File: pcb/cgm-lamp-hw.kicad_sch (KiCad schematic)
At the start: 55 parts, among them J1 USB_C_Receptacle_USB2.0_14P, J2 Conn_01x02, J3 DNP, Q1 DMG2305, SW1 RotaryEncoder_Switch_MP, SW2 SW_Push, SW3 SW_Push, SW4 SW_SPST, U1 RT9080-33GJ5, U2 MCP73831-2-OT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

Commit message: Assign footprints, start layout
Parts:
- C1, C10, C11, C2, C3, C4, C5, C6, C7, C8, C9: footprint (none) -> Capacitor_SMD:C_0603_1608Metric_Pad1.08x0.95mm_HandSolder
- D10: footprint (none) -> Diode_SMD:D_SOD-323_HandSoldering
- D11, D12, D13, D9: footprint (none) -> LED_SMD:LED_1206_3216Metric_Pad1.42x1.75mm_HandSolder
- J1: footprint (none) -> Connector_USB:USB_C_Receptacle_GCT_USB4105-xx-A_16P_TopMnt_Horizontal
- J2: footprint (none) -> Connector_JST:JST_PH_S2B-PH-SM4-TB_1x02-1MP_P2.00mm_Horizontal
- J3: footprint (none) -> Connector_PinHeader_2.54mm:PinHeader_1x03_P2.54mm_Vertical
- R1, R10, R11, R12, R13, R14, R15, R16, R17, R2, R3, R4, R5, R6, R7, R8, R9: footprint (none) -> Resistor_SMD:R_0603_1608Metric_Pad0.98x0.95mm_HandSolder
- SW1: footprint (none) -> Rotary_Encoder:RotaryEncoder_Bourns_Vertical_PEC12R-3x17F-Sxxxx
- SW2, SW3: footprint (none) -> Button_Switch_SMD:SW_SPST_PTS645
- SW4: footprint (none) -> Button_Switch_THT:SW_E-Switch_EG2219_DPDT_Angled
- TP1, TP2: footprint (none) -> TestPoint:TestPoint_Loop_D2.54mm_Drill1.5mm_Beaded
- U1: footprint RT9080-33GJ5:SOT94P280X100-5N -> SnapEDA:SOT94P280X100-5N
- U3: footprint ESP32-C6-WROOM-1-N8:XCVR_ESP32-C6-WROOM-1-N8 -> SnapEDA:XCVR_ESP32-C6-WROOM-1-N8
- U4: footprint MAX17048G_T10:SON50P200X200X80-9N -> SnapEDA:SON50P200X200X80-9N
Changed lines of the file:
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@@
 			)
 		)
-		(property "Footprint" ""
+		(property "Footprint" "Resistor_SMD:R_0603_1608Metric_Pad0.98x0.95mm_HandSolder"
 			(at 99.822 144.78 90)
 			(effects
@@
 			)
 		)
-		(property "Footprint" ""
+		(property "Footprint" "Resistor_SMD:R_0603_1608Metric_Pad0.98x0.95mm_HandSolder"
 			(at 140.208 179.07 90)
 			(effects
@@
 			)
 		)
-		(property "Footprint" ""
+		(property "Footprint" "Resistor_SMD:R_0603_1608Metric_Pad0.98x0.95mm_HandSolder"
 			(at 215.138 48.26 90)
 			(effects
@@
 			)
 		)
-		(property "Footprint" ""
+		(property "Footprint" "LED_SMD:LED_1206_3216Metric_Pad1.42x1.75mm_HandSolder"
 			(at 138.43 187.96 0)
 			(effects
@@
 			)
 		)
-		(property "Footprint" ""
+		(property "Footprint" "Resistor_SMD:R_0603_1608Metric_Pad0.98x0.95mm_HandSolder"
 			(at 51.562 36.83 90)
 			(effects
@@
 			)
 		)
-		(property "Footprint" ""
+		(property "Footprint" "Resistor_SMD:R_0603_1608Metric_Pad0.98x0.95mm_HandSolder"
 			(at 173.228 140.97 90)
 			(effects
@@
 			)
 		)
-		(property "Footprint" ""
+		(property "Footprint" "Resistor_SMD:R_0603_1608Metric_Pad0.98x0.95mm_HandSolder"
 			(at 166.878 179.07 90)
 			(effects
@@
 			)
 		)
-		(property "Footprint" ""
+		(property "Footprint" "Resistor_SMD:R_0603_1608Metric_Pad0.98x0.95mm_HandSolder"
 			(at 104.648 187.96 90)
 			(effects
@@
 			)
 		)
-		(property "Footprint" ""
+		(property "Footprint" "Resistor_SMD:R_0603_1608Metric_Pad0.98x0.95mm_HandSolder"
 			(at 118.11 52.578 90)
 			(effects
@@
 			)
 		)
-		(property "Footprint" ""
+		(property "Footprint" "LED_SMD:LED_1206_3216Metric_Pad1.42x1.75mm_HandSolder"
 			(at 165.1 187.96 0)
 			(effects
@@
 			)
 		)
-		(property "Footprint" ""
+		(property "Footprint" "Resistor_SMD:R_0603_1608Metric_Pad0.98x0.95mm_HandSolder"
 			(at 117.348 187.96 90)
 			(effects
@@
 			)
 		)
-		(property "Footprint" ""
+		(property "Footprint" "Resistor_SMD:R_0603_1608Metric_Pad0.98x0.95mm_HandSolder"
 			(at 168.91 88.392 90)
 			(effects
@@
 			)
 		)
-		(property "Footprint" ""
+		(property "Footprint" "LED_SMD:LED_1206_3216Metric_Pad1.42x1.75mm_HandSolder"
 			(at 201.93 48.26 0)
 			(effects
@@
 			)
 		)
-		(property "Footprint" ""
+		(property "Footprint" "Capacitor_SMD:C_0603_1608Metric_Pad1.08x0.95mm_HandSolder"
 			(at 225.7552 101.6 0)
 			(effects
@@
 			)
 		)
-		(property "Footprint" ""
+		(property "Footprint" "Resistor_SMD:R_0603_1608Metric_Pad0.98x0.95mm_HandSolder"
 			(at 243.078 48.26 90)
 			(effects
@@
 			)
 		)
-		(property "Footprint" ""
+		(property "Footprint" "Diode_SMD:D_SOD-323_HandSoldering"
 			(at 96.52 45.72 0)
 			(effects
@@
 			)
 		)
-		(property "Footprint" ""
+		(property "Footprint" "Button_Switch_THT:SW_E-Switch_EG2219_DPDT_Angled"
 			(at 250.19 152.4 0)
 			(effects
@@
 			)
 		)
-		(property "Footprint" ""
+		(property "Footprint" "Button_Switch_SMD:SW_SPST_PTS645"
 			(at 166.37 152.4 0)
 			(effects
@@
 			)
 		)
-		(property "Footprint" "ESP32-C6-WROOM-1-N8:XCVR_ESP32-C6-WROOM-1-N8"
+		(property "Footprint" "SnapEDA:XCVR_ESP32-C6-WROOM-1-N8"
 			(at 128.27 109.22 0)
 			(effects
@@
 			)
 		)
-		(property "Footprint" ""
+		(property "Footprint" "Capacitor_SMD:C_0603_1608Metric_Pad1.08x0.95mm_HandSolder"
 			(at 186.3852 156.21 0)
 			(effects
@@
 			)
 		)
-		(property "Footprint" ""
+		(property "Footprint" "Connector_USB:USB_C_Receptacle_GCT_USB4105-xx-A_16P_TopMnt_Horizontal"
 			(at 33.02 40.64 0)
 			(effects
@@
 			)
 		)
-		(property "Footprint" ""
+		(property "Footprint" "Connector_JST:JST_PH_S2B-PH-SM4-TB_1x02-1MP_P2.00mm_Horizontal"
 			(at 266.7 38.1 0)
 			(effects
@@
 			)
 		)
-		(property "Footprint" ""
+		(property "Footprint" "TestPoint:TestPoint_Loop_D2.54mm_Drill1.5mm_Beaded"
 			(at 149.86 111.76 0)
 			(effects
@@
 			)
 		)
-		(property "Footprint" ""
+		(property "Footprint" "Resistor_SMD:R_0603_1608Metric_Pad0.98x0.95mm_HandSolder"
 			(at 202.692 104.14 90)
 			(effects
@@
 			)
 		)
-		(property "Footprint" ""
+		(property "Footprint" "Resistor_SMD:R_0603_1608Metric_Pad0.98x0.95mm_HandSolder"
 			(at 87.122 52.07 90)
 			(effects
@@
 			)
 		)
-		(property "Footprint" "RT9080-33GJ5:SOT94P280X100-5N"
+		(property "Footprint" "SnapEDA:SOT94P280X100-5N"
 			(at 123.19 45.72 0)
 			(effects
@@
 			)
 		)
-		(property "Footprint" ""
+		(property "Footprint" "Capacitor_SMD:C_0603_1608Metric_Pad1.08x0.95mm_HandSolder"
 			(at 108.9152 55.88 0)
 			(effects
@@
 			)
 		)
-		(property "Footprint" ""
+		(property "Footprint" "Button_Switch_SMD:SW_SPST_PTS645"
 			(at 205.74 152.4 0)
 			(effects
@@
 			)
 		)
-		(property "Footprint" ""
+		(property "Footprint" "Resistor_SMD:R_0603_1608Metric_Pad0.98x0.95mm_HandSolder"
 			(at 154.178 179.07 90)
 			(effects
@@
 			)
 		)
-		(property "Footprint" ""
+		(property "Footprint" "Connector_PinHeader_2.54mm:PinHeader_1x03_P2.54mm_Vertical"
 			(at 16.51 153.67 0)
 			(effects
@@
 			)
 		)
-		(property "Footprint" ""
+		(property "Footprint" "Resistor_SMD:R_0603_1608Metric_Pad0.98x0.95mm_HandSolder"
 			(at 268.732 85.09 90)
 			(effects
@@
 			)
 		)
-		(property "Footprint" ""
+		(property "Footprint" "LED_SMD:LED_1206_3216Metric_Pad1.42x1.75mm_HandSolder"
 			(at 152.4 187.96 0)
 			(effects
@@
 			)
 		)
-		(property "Footprint" ""
+		(property "Footprint" "Capacitor_SMD:C_0603_1608Metric_Pad1.08x0.95mm_HandSolder"
 			(at 191.4652 46.99 0)
 			(effects
@@
 			)
 		)
-		(property "Footprint" ""
+		(property "Footprint" "Resistor_SMD:R_0603_1608Metric_Pad0.98x0.95mm_HandSolder"
 			(at 64.262 36.83 90)
 			(effects
@@
 			)
 		)
-		(property "Footprint" ""
+		(property "Footprint" "Capacitor_SMD:C_0603_1608Metric_Pad1.08x0.95mm_HandSolder"
 			(at 174.2948 91.44 0)
 			(effects
@@
 			)
 		)
-		(property "Footprint" ""
+		(property "Footprint" "Rotary_Encoder:RotaryEncoder_Bourns_Vertical_PEC12R-3x17F-Sxxxx"
 			(at 183.896 105.41 0)
 			(effects
@@
 			)
 		)
-		(property "Footprint" ""
+		(property "Footprint" "Capacitor_SMD:C_0603_1608Metric_Pad1.08x0.95mm_HandSolder"
 			(at 252.4252 52.07 0)
 			(effects
@@
 			)
 		)
-		(property "Footprint" ""
+		(property "Footprint" "Capacitor_SMD:C_0603_1608Metric_Pad1.08x0.95mm_HandSolder"
 			(at 165.4048 110.49 0)
 			(effects
@@
 			)
 		)
-		(property "Footprint" ""
+		(property "Footprint" "TestPoint:TestPoint_Loop_D2.54mm_Drill1.5mm_Beaded"
 			(at 149.86 114.3 0)
 			(effects
@@
 			)
 		)
-		(property "Footprint" "MAX17048G_T10:SON50P200X200X80-9N"
+		(property "Footprint" "SnapEDA:SON50P200X200X80-9N"
 			(at 250.19 104.14 0)
 			(effects
@@
 			)
 		)
-		(property "Footprint" ""
+		(property "Footprint" "Capacitor_SMD:C_0603_1608Metric_Pad1.08x0.95mm_HandSolder"
 			(at 266.3952 156.21 0)
 			(effects
@@
 			)
 		)
-		(property "Footprint" ""
+		(property "Footprint" "Resistor_SMD:R_0603_1608Metric_Pad0.98x0.95mm_HandSolder"
 			(at 164.592 104.14 90)
 			(effects
@@
 			)
 		)
-		(property "Footprint" ""
+		(property "Footprint" "Capacitor_SMD:C_0603_1608Metric_Pad1.08x0.95mm_HandSolder"
 			(at 225.7552 156.21 0)
 			(effects
@@
 			)
 		)
-		(property "Footprint" ""
+		(property "Footprint" "Capacitor_SMD:C_0603_1608Metric_Pad1.08x0.95mm_HandSolder"
 			(at 203.5048 110.49 0)
 			(effects
@@
 			)
 		)
-		(property "Footprint" ""
+		(property "Footprint" "Capacitor_SMD:C_0603_1608Metric_Pad1.08x0.95mm_HandSolder"
 			(at 158.4452 55.88 0)
 			(effects

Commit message: Add dru, more layout
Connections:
- net ENC_A: now also U3.16 (IO18); no longer U3.27 (IO2)
- net ENC_B: now also U3.17 (IO19); no longer U3.26 (IO3)
- net ENC_BTN: now also U3.14 (IO13); no longer U3.9 (IO1)
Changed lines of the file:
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@@
+	)
+	(no_connect
+		(at 107.95 106.68)
 	)
 	(no_connect
@@
 	)
 	(no_connect
-		(at 148.59 101.6)
-	)
-	(no_connect
-		(at 148.59 114.3)
-	)
-	(no_connect
 		(at 107.95 99.06)
 	)
@@
 	)
 	(no_connect
-		(at 148.59 111.76)
+		(at 107.95 101.6)
+	)
+	(no_connect
+		(at 107.95 104.14)
 	)
 	(no_connect
@@
 		)
 	)
+	(wire
+		(pts
+			(xy 148.59 114.3) (xy 157.48 114.3)
+		)
+		(stroke
+			(width 0)
+			(type default)
+		)
+	)
 	(polyline
 		(pts
@@
 	(wire
 		(pts
-			(xy 99.06 101.6) (xy 107.95 101.6)
-		)
-		(stroke
-			(width 0)
-			(type default)
-		)
-	)
-	(wire
-		(pts
-			(xy 99.06 104.14) (xy 107.95 104.14)
+			(xy 148.59 111.76) (xy 157.48 111.76)
 		)
 		(stroke
@@
 	(wire
 		(pts
-			(xy 99.06 106.68) (xy 107.95 106.68)
-		)
-		(stroke
-			(width 0)
-			(type default)
-		)
-	)
-	(wire
-		(pts
 			(xy 97.79 195.58) (xy 102.87 195.58)
 		)
@@
 		(pts
 			(xy 274.32 104.14) (xy 267.97 104.14)
+		)
+		(stroke
+			(width 0)
+			(type default)
+		)
+	)
+	(wire
+		(pts
+			(xy 148.59 101.6) (xy 157.48 101.6)
 		)
 		(stroke
@@
 	(label "CHG"
 		(at 99.06 109.22 0)
+		(fields_autoplaced yes)
 		(effects
 			(font
@@
 	(label "ENC_B"
 		(at 190.5 118.11 90)
+		(fields_autoplaced yes)
 		(effects
 			(font
@@
 	(label "VREG_EN"
 		(at 274.32 146.05 180)
+		(fields_autoplaced yes)
 		(effects
 			(font
@@
 	(label "BOOT"
 		(at 232.41 146.05 180)
+		(fields_autoplaced yes)
 		(effects
 			(font
@@
 	(label "RGB"
 		(at 107.95 151.13 180)
+		(fields_autoplaced yes)
 		(effects
 			(font
@@
 	)
 	(label "ENC_BTN"
-		(at 99.06 101.6 0)
-		(effects
-			(font
-				(size 1.27 1.27)
-			)
-			(justify left bottom)
+		(at 157.48 101.6 180)
+		(fields_autoplaced yes)
+		(effects
+			(font
+				(size 1.27 1.27)
+			)
+			(justify right bottom)
 		)
 	)
 	(label "RGB"
 		(at 99.06 119.38 0)
+		(fields_autoplaced yes)
 		(effects
 			(font
@@
 	(label "D+"
 		(at 157.48 99.06 180)
+		(fields_autoplaced yes)
 		(effects
 			(font
@@
 	(label "ALERT"
 		(at 157.48 172.72 180)
+		(fields_autoplaced yes)
 		(effects
 			(font
@@
 	(label "D-"
 		(at 48.26 39.37 180)
+		(fields_autoplaced yes)
 		(effects
 			(font
@@
 	(label "ALERT"
 		(at 279.4 91.44 180)
+		(fields_autoplaced yes)
 		(effects
 			(font
@@
 	(label "VREG_EN"
 		(at 114.3 54.61 0)
+		(fields_autoplaced yes)
 		(effects
 			(font
@@
 	(label "SDA"
 		(at 99.06 114.3 0)
+		(fields_autoplaced yes)
 		(effects
 			(font
@@
 	(label "VBAT"
 		(at 217.17 91.44 0)
+		(fields_autoplaced yes)
 		(effects
 			(font
@@
 	(label "RGB"
 		(at 26.67 156.21 180)
+		(fields_autoplaced yes)
 		(effects
 			(font
@@
 	(label "ESP_EN"
 		(at 193.04 146.05 180)
+		(fields_autoplaced yes)
 		(effects
 			(font
@@
 	(label "SCL"
 		(at 99.06 116.84 0)
+		(fields_autoplaced yes)
 		(effects
 			(font
@@
 	(label "SDA"
 		(at 97.79 195.58 0)
+		(fields_autoplaced yes)
 		(effects
 			(font
@@
 	)
 	(label "ENC_B"
-		(at 99.06 106.68 0)
-		(effects
-			(font
-				(size 1.27 1.27)
-			)
-			(justify left bottom)
+		(at 157.48 114.3 180)
+		(fields_autoplaced yes)
+		(effects
+			(font
+				(size 1.27 1.27)
+			)
+			(justify right bottom)
 		)
 	)
 	(label "ENC_A"
-		(at 99.06 104.14 0)
-		(effects
-			(font
-				(size 1.27 1.27)
-			)
-			(justify left bottom)
+		(at 157.48 111.76 180)
+		(fields_autoplaced yes)
+		(effects
+			(font
+				(size 1.27 1.27)
+			)
+			(justify right bottom)
 		)
 	)
 	(label "VBAT"
 		(at 104.14 25.4 0)
+		(fields_autoplaced yes)
 		(effects
 			(font
@@
 	(label "ENC_BTN"
 		(at 194.31 90.17 180)
+		(fields_autoplaced yes)
 		(effects
 			(font
@@
 	(label "SCL"
 		(at 274.32 104.14 180)
+		(fields_autoplaced yes)
 		(effects
 			(font
@@
 	(label "D+"
 		(at 48.26 44.45 180)
+		(fields_autoplaced yes)
 		(effects
 			(font
@@
 	(label "IND"
 		(at 170.18 172.72 180)
+		(fields_autoplaced yes)
 		(effects
 			(font
@@
 	(label "CHG"
 		(at 207.01 43.18 0)
+		(fields_autoplaced yes)
 		(effects
 			(font
@@
 	(label "SCL"
 		(at 110.49 195.58 0)
+		(fields_autoplaced yes)
 		(effects
 			(font
@@
 	(label "SDA"
 		(at 274.32 101.6 180)
+		(fields_autoplaced yes)
 		(effects
 			(font
@@
 	(label "BOOT"
 		(at 99.06 121.92 0)
+		(fields_autoplaced yes)
 		(effects
 			(font
@@
 	(label "ENC_A"
 		(at 185.42 118.11 90)
+		(fields_autoplaced yes)
 		(effects
 			(font
@@
 	(label "D-"
 		(at 157.48 96.52 180)
+		(fields_autoplaced yes)
 		(effects
 			(font
@@
 	(label "IND"
 		(at 99.06 111.76 0)
+		(fields_autoplaced yes)
 		(effects
 			(font
@@
 	(label "ESP_EN"
 		(at 99.06 93.98 0)
+		(fields_autoplaced yes)
 		(effects
 			(font
@@
 	(label "VBAT"
 		(at 259.08 38.1 180)
+		(fields_autoplaced yes)
 		(effects
 			(font
@@
 	(label "RGB"
 		(at 16.51 91.44 0)
-		(effects
-			(font
+		(fields_autoplaced yes)
+		(effects
+			(font

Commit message: Added moutning holes
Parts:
- added H1, H2, H3, H4: MountingHole, symbol Mechanical:MountingHole

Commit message: Added title
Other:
- title: (none) -> CGM Lamp
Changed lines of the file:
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@@
 	(generator_version "8.0")
 	(paper "A4")
+	(title_block
+		(title "CGM Lamp")
+		(rev "1")
+	)
 	(junction
 		(at 204.47 109.22)
@@
 	(label "CHG"
 		(at 99.06 109.22 0)
+		(fields_autoplaced yes)
 		(effects
 			(font
@@
 	(label "ENC_B"
 		(at 190.5 118.11 90)
+		(fields_autoplaced yes)
 		(effects
 			(font
@@
 	(label "VREG_EN"
 		(at 274.32 146.05 180)
+		(fields_autoplaced yes)
 		(effects
 			(font
@@
 	(label "BOOT"
 		(at 232.41 146.05 180)
+		(fields_autoplaced yes)
 		(effects
 			(font
@@
 	(label "RGB"
 		(at 107.95 151.13 180)
+		(fields_autoplaced yes)
 		(effects
 			(font
@@
 	(label "ENC_BTN"
 		(at 157.48 101.6 180)
+		(fields_autoplaced yes)
 		(effects
 			(font
@@
 	(label "RGB"
 		(at 99.06 119.38 0)
+		(fields_autoplaced yes)
 		(effects
 			(font
@@
 	(label "D+"
 		(at 157.48 99.06 180)
+		(fields_autoplaced yes)
 		(effects
 			(font
@@
 	(label "ALERT"
 		(at 157.48 172.72 180)
+		(fields_autoplaced yes)
 		(effects
 			(font
@@
 	(label "D-"
 		(at 48.26 39.37 180)
+		(fields_autoplaced yes)
 		(effects
 			(font
@@
 	(label "ALERT"
 		(at 279.4 91.44 180)
+		(fields_autoplaced yes)
 		(effects
 			(font
@@
 	(label "VREG_EN"
 		(at 114.3 54.61 0)
+		(fields_autoplaced yes)
 		(effects
 			(font
@@
 	(label "SDA"
 		(at 99.06 114.3 0)
+		(fields_autoplaced yes)
 		(effects
 			(font
@@
 	(label "VBAT"
 		(at 217.17 91.44 0)
+		(fields_autoplaced yes)
 		(effects
 			(font
@@
 	(label "RGB"
 		(at 26.67 156.21 180)
+		(fields_autoplaced yes)
 		(effects
 			(font
@@
 	(label "ESP_EN"
 		(at 193.04 146.05 180)
+		(fields_autoplaced yes)
 		(effects
 			(font
@@
 	(label "SCL"
 		(at 99.06 116.84 0)
+		(fields_autoplaced yes)
 		(effects
 			(font
@@
 	(label "SDA"
 		(at 97.79 195.58 0)
+		(fields_autoplaced yes)
 		(effects
 			(font
@@
 	(label "ENC_B"
 		(at 157.48 114.3 180)
+		(fields_autoplaced yes)
 		(effects
 			(font
@@
 	(label "ENC_A"
 		(at 157.48 111.76 180)
+		(fields_autoplaced yes)
 		(effects
 			(font
@@
 	(label "VBAT"
 		(at 104.14 25.4 0)
+		(fields_autoplaced yes)
 		(effects
 			(font
@@
 	(label "ENC_BTN"
 		(at 194.31 90.17 180)
+		(fields_autoplaced yes)
 		(effects
 			(font
@@
 	(label "SCL"
 		(at 274.32 104.14 180)
+		(fields_autoplaced yes)
 		(effects
 			(font
@@
 	(label "D+"
 		(at 48.26 44.45 180)
+		(fields_autoplaced yes)
 		(effects
 			(font
@@
 	(label "IND"
 		(at 170.18 172.72 180)
+		(fields_autoplaced yes)
 		(effects
 			(font
@@
 	(label "CHG"
 		(at 207.01 43.18 0)
+		(fields_autoplaced yes)
 		(effects
 			(font
@@
 	(label "SCL"
 		(at 110.49 195.58 0)
+		(fields_autoplaced yes)
 		(effects
 			(font
@@
 	(label "SDA"
 		(at 274.32 101.6 180)
+		(fields_autoplaced yes)
 		(effects
 			(font
@@
 	(label "BOOT"
 		(at 99.06 121.92 0)
+		(fields_autoplaced yes)
 		(effects
 			(font
@@
 	(label "ENC_A"
 		(at 185.42 118.11 90)
+		(fields_autoplaced yes)
 		(effects
 			(font
@@
 	(label "D-"
 		(at 157.48 96.52 180)
+		(fields_autoplaced yes)
 		(effects
 			(font
@@
 	(label "IND"
 		(at 99.06 111.76 0)
+		(fields_autoplaced yes)
 		(effects
 			(font
@@
 	(label "ESP_EN"
 		(at 99.06 93.98 0)
+		(fields_autoplaced yes)
 		(effects
 			(font
@@
 	(label "VBAT"
 		(at 259.08 38.1 180)
+		(fields_autoplaced yes)
 		(effects
 			(font
@@
 	(label "RGB"
 		(at 16.51 91.44 0)
-		(effects
-			(font
+		(fields_autoplaced yes)
+		(effects
+			(font

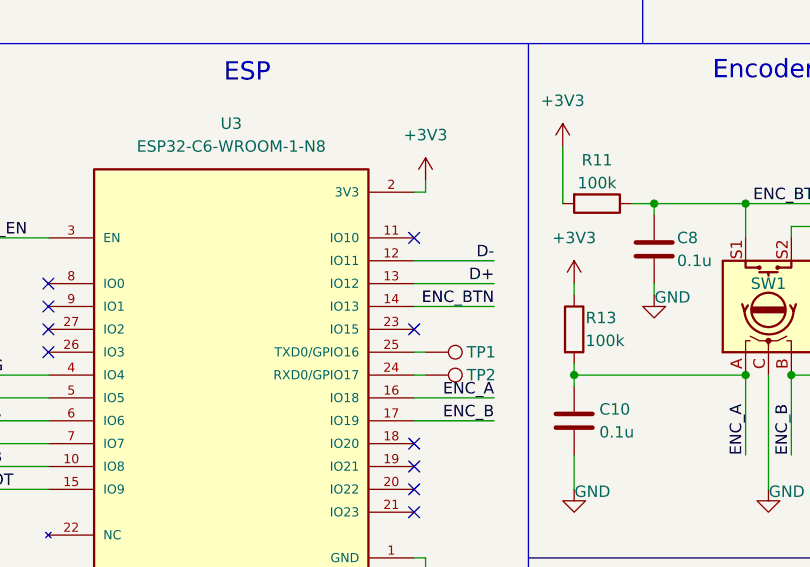
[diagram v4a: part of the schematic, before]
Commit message: Bump rev, fix usb pin assignment
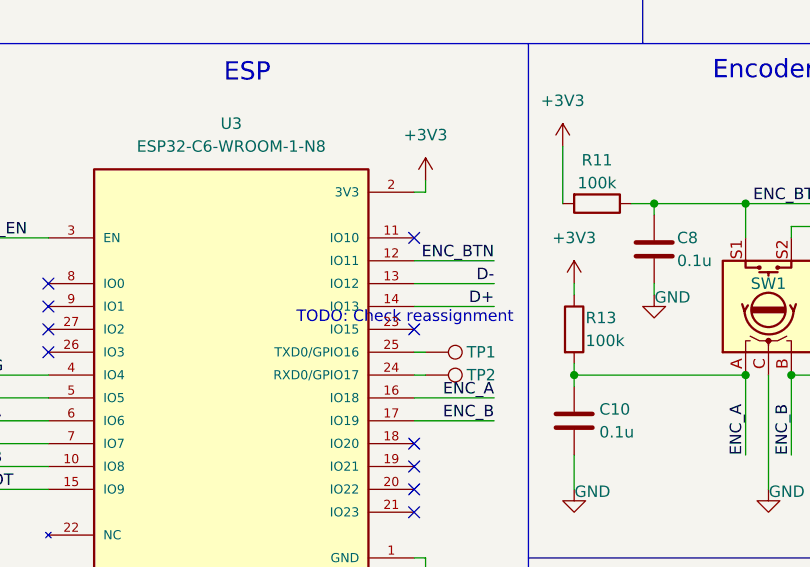
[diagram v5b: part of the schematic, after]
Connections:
- net D+: now also U3.14 (IO13); no longer U3.13 (IO12)
- net D-: now also U3.13 (IO12); no longer U3.12 (IO11)
- net ENC_BTN: now also U3.12 (IO11); no longer U3.14 (IO13)
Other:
- note added: "TODO: Check reassignment"
